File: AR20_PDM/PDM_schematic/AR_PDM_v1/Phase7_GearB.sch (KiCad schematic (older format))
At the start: 12 parts, among them Q7 BTS50025-1TAD, U11 INA233

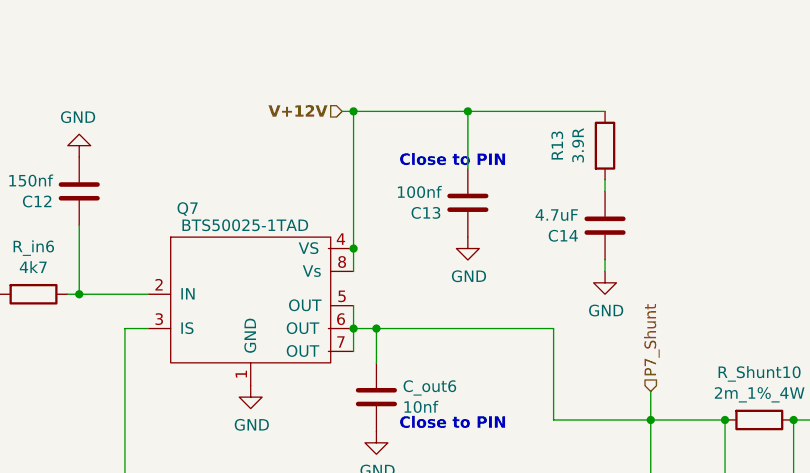
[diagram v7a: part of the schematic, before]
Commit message: First Complete Draft of PCB and schematics, - minus see discription
- missing correct smd switch header
- missing correct main power plug
- tweeks still needs to be done
- Extra inspection of schematics pending
- proper, in depth quiality controll of pcb work pending
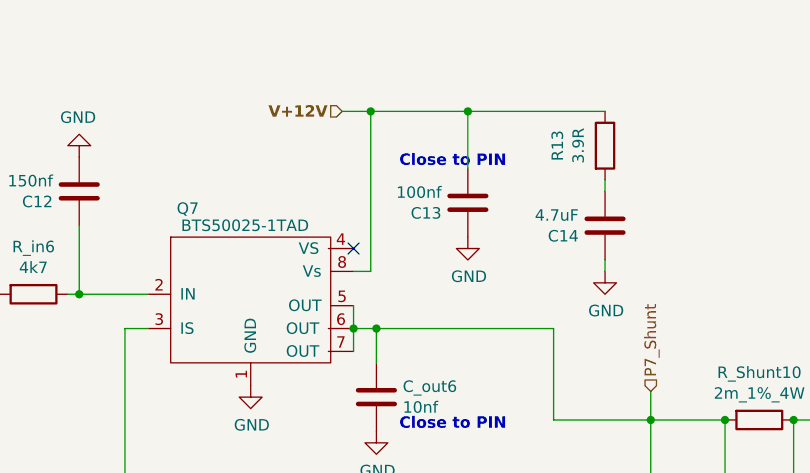
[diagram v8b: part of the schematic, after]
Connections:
- net V+12V: no longer Q7.4 (VS)
- no-connect marks 0 -> 1
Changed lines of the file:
@@
 $Descr A4 11693 8268
 encoding utf-8
-Sheet 9 13
+Sheet 8 13
 Title ""
 Date ""
@@
 	4700 2550 4700 2450
 Wire Wire Line
-	4650 1600 4700 1600
-Wire Wire Line
-	4700 2300 4700 2200
-Wire Wire Line
-	4700 2200 4700 1600
-Connection ~ 4700 2200
-Connection ~ 4700 1600
-Wire Wire Line
-	4700 1600 5200 1600
-Wire Wire Line
 	6000 2950 6000 2825
 Text HLabel 6000 2825 1    50   Input ~ 0
@@
 Text HLabel 3700 3850 3    50   Output ~ 0
 P7_MOS_SENSE
+Wire Wire Line
+	4650 1600 4775 1600
+Wire Wire Line
+	4775 2300 4700 2300
+Wire Wire Line
+	4775 1600 4775 2300
+NoConn ~ 4700 2200
+Connection ~ 4775 1600
+Wire Wire Line
+	4775 1600 5200 1600
 $EndSCHEMATC
